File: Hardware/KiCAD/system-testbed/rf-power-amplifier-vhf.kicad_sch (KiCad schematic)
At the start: 22 parts, among them U14 GRF5604

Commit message: feat: assign 0603 passive component footprints #32 #34
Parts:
- C63, C64, C65, C66, C67, C68, C69, C70, C71, C72, C73, C74, C75, C76: footprint (none) -> Capacitor_SMD:C_0603_1608Metric
- L15, L16, L17: footprint (none) -> Inductor_SMD:L_0603_1608Metric
- R16, R17, R18: footprint (none) -> Resistor_SMD:R_0603_1608Metric
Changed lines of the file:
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@@
 			)
 		)
-		(property "Footprint" ""
+		(property "Footprint" "Capacitor_SMD:C_0603_1608Metric"
 			(at 205.74 77.47 0)
 			(effects
@@
 			)
 		)
-		(property "Footprint" ""
+		(property "Footprint" "Inductor_SMD:L_0603_1608Metric"
 			(at 71.12 83.82 0)
 			(effects
@@
 			)
 		)
-		(property "Footprint" ""
+		(property "Footprint" "Resistor_SMD:R_0603_1608Metric"
 			(at 87.884 32.766 90)
 			(effects
@@
 			)
 		)
-		(property "Footprint" ""
+		(property "Footprint" "Capacitor_SMD:C_0603_1608Metric"
 			(at 144.78 83.82 0)
 			(effects
@@
 			)
 		)
-		(property "Footprint" ""
+		(property "Footprint" "Capacitor_SMD:C_0603_1608Metric"
 			(at 158.75 77.47 0)
 			(effects
@@
 			)
 		)
-		(property "Footprint" ""
+		(property "Footprint" "Inductor_SMD:L_0603_1608Metric"
 			(at 144.78 71.12 0)
 			(effects
@@
 			)
 		)
-		(property "Footprint" ""
+		(property "Footprint" "Resistor_SMD:R_0603_1608Metric"
 			(at 138.684 63.754 90)
 			(effects
@@
 			)
 		)
-		(property "Footprint" ""
+		(property "Footprint" "Capacitor_SMD:C_0603_1608Metric"
 			(at 104.14 45.72 0)
 			(effects
@@
 			)
 		)
-		(property "Footprint" ""
+		(property "Footprint" "Capacitor_SMD:C_0603_1608Metric"
 			(at 171.45 43.18 0)
 			(effects
@@
 			)
 		)
-		(property "Footprint" ""
+		(property "Footprint" "Capacitor_SMD:C_0603_1608Metric"
 			(at 176.53 83.82 0)
 			(effects
@@
 			)
 		)
-		(property "Footprint" ""
+		(property "Footprint" "Capacitor_SMD:C_0603_1608Metric"
 			(at 73.66 45.72 0)
 			(effects
@@
 			)
 		)
-		(property "Footprint" ""
+		(property "Footprint" "Capacitor_SMD:C_0603_1608Metric"
 			(at 165.1 83.82 0)
 			(effects
@@
 			)
 		)
-		(property "Footprint" ""
+		(property "Footprint" "Capacitor_SMD:C_0603_1608Metric"
 			(at 161.29 43.18 0)
 			(effects
@@
 			)
 		)
-		(property "Footprint" ""
+		(property "Footprint" "Capacitor_SMD:C_0603_1608Metric"
 			(at 199.39 83.82 0)
 			(effects
@@
 			)
 		)
-		(property "Footprint" ""
+		(property "Footprint" "Capacitor_SMD:C_0603_1608Metric"
 			(at 187.96 83.82 0)
 			(effects
@@
 			)
 		)
-		(property "Footprint" ""
+		(property "Footprint" "Capacitor_SMD:C_0603_1608Metric"
 			(at 88.9 45.72 0)
 			(effects
@@
 			)
 		)
-		(property "Footprint" ""
+		(property "Footprint" "Capacitor_SMD:C_0603_1608Metric"
 			(at 87.63 77.47 0)
 			(effects
@@
 			)
 		)
-		(property "Footprint" ""
+		(property "Footprint" "Resistor_SMD:R_0603_1608Metric"
 			(at 72.644 32.766 90)
 			(effects
@@
 			)
 		)
-		(property "Footprint" ""
+		(property "Footprint" "Inductor_SMD:L_0603_1608Metric"
 			(at 114.3 45.72 0)
 			(effects
@@
 			)
 		)
-		(property "Footprint" ""
+		(property "Footprint" "Capacitor_SMD:C_0603_1608Metric"
 			(at 77.47 77.47 0)
 			(effects

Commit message: fix: import RF sheet contents #65
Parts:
- renumbered C63 to C56, C64 to C57, C65 to C58, C66 to C59, C67 to C60, C68 to C61, C69 to C62, C70 to C63, C71 to C64, C72 to C65, C73 to C66, C74 to C67, C75 to C68, C76 to C69, L15 to L22, L16 to L23, L17 to L24, U14 to U4

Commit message: fix: reannotate schematics for pcb editor use #55
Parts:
- L36: renamed from L22; footprint Inductor_SMD:L_0603_1608Metric -> Inductor_SMD:L_0402_1005Metric
- L37: renamed from L23; footprint Inductor_SMD:L_0603_1608Metric -> Inductor_SMD:L_0402_1005Metric
- L38: renamed from L24; footprint Inductor_SMD:L_0603_1608Metric -> Inductor_SMD:L_0402_1005Metric
- renumbered C56 to C80, C57 to C81, C58 to C82, C59 to C83, C60 to C84, C61 to C85, C62 to C86, C63 to C87, C64 to C88, C65 to C89, C66 to C90, C67 to C91, C68 to C92, C69 to C93, JP10 to JP9, R16 to R17, R17 to R18, R18 to R19, U4 to U6

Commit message: fix: allow for DRC use in PCB editor by successful reannotation
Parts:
- C80, C81, C82, C83, C84, C85, C87, C88, C89, C90, C91, C92, C93: footprint Capacitor_SMD:C_0603_1608Metric -> Capacitor_SMD:C_0402_1005Metric
- L86: renamed from C86; footprint Capacitor_SMD:C_0603_1608Metric -> Inductor_SMD:L_0402_1005Metric
- R17, R18, R19: footprint Resistor_SMD:R_0603_1608Metric -> Resistor_SMD:R_0402_1005Metric
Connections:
- net +5V renamed +3.3V

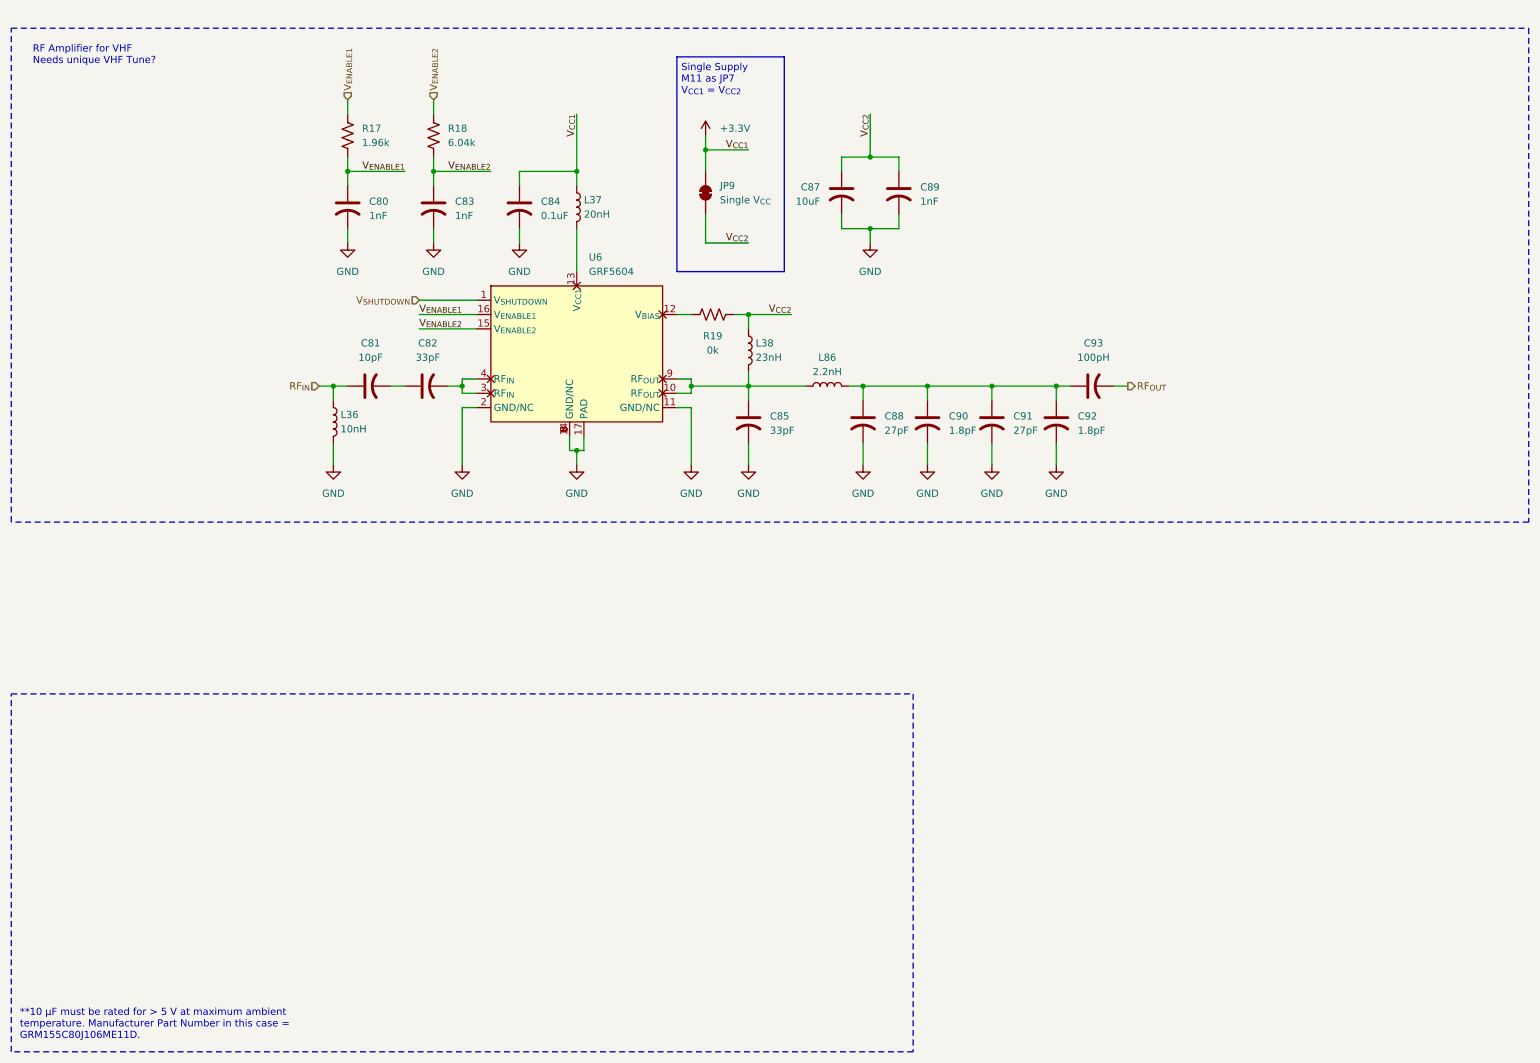
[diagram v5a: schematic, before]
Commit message: feat: separate RF subsystems for testing using SMA edge launches in testbed KiCAD project #65 #34 #45
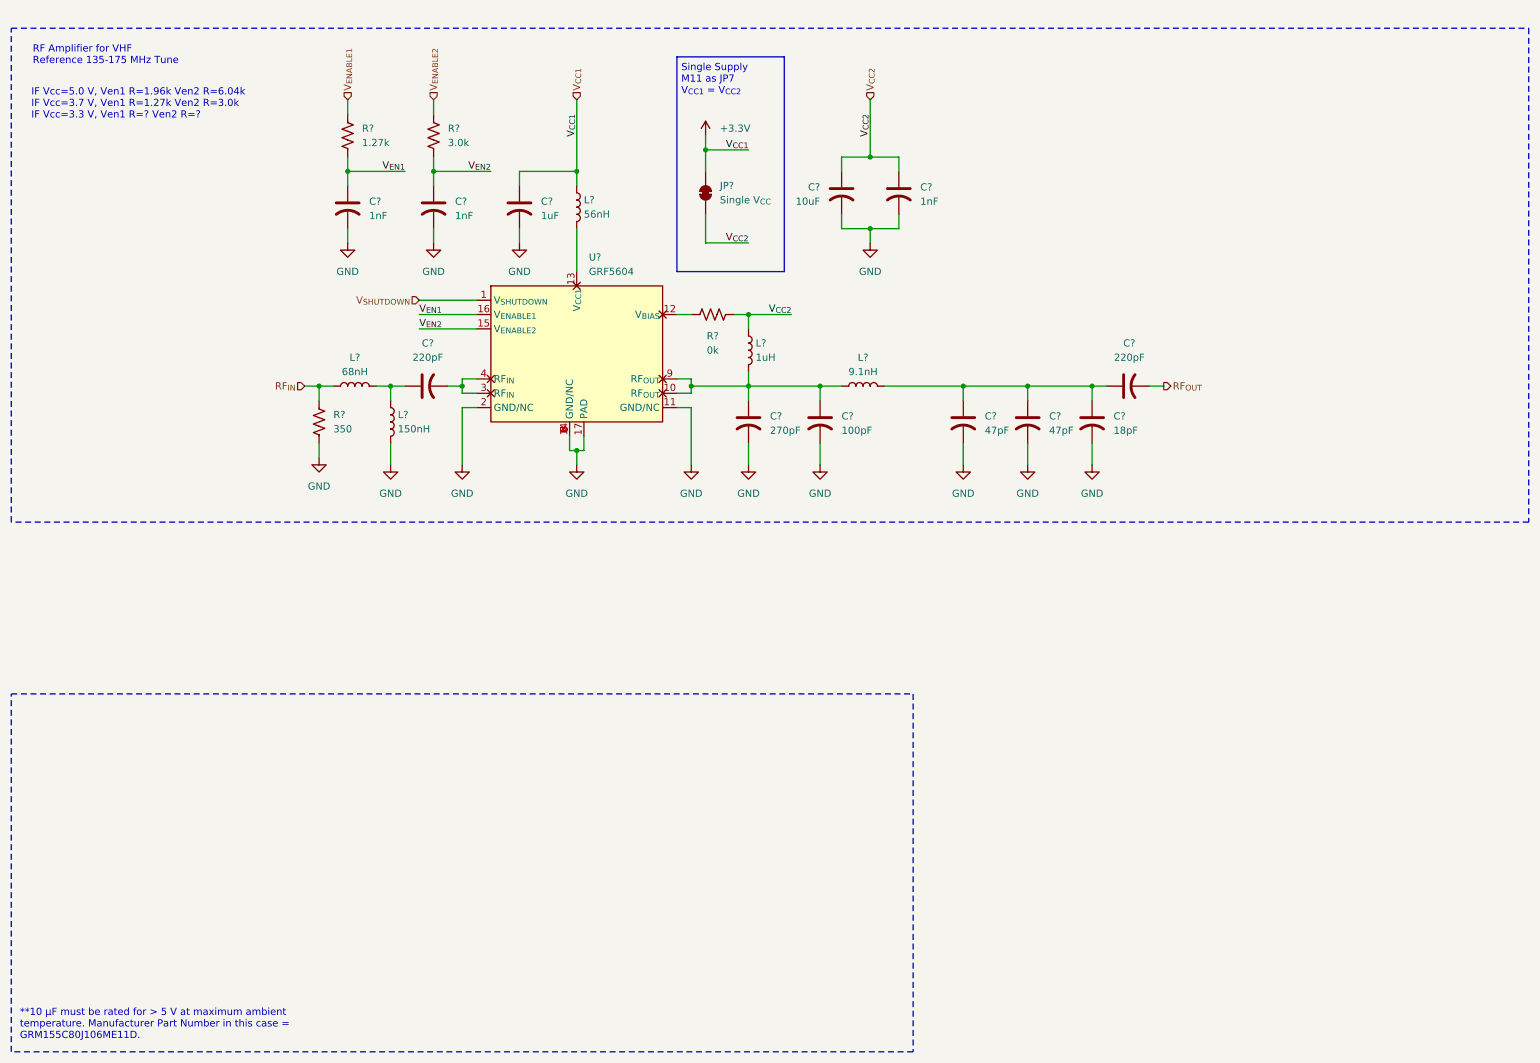
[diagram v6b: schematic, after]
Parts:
- added R?: 350, Resistor_SMD:R_0402_1005Metric, symbol Device:R_US
- C?: renamed from C93; value 100pH -> 220pF
- C?: renamed from C85; value 33pF -> 270pF
- C?: renamed from C84; value 0.1uF -> 1uF
- C?: renamed from C90; value 1.8pF -> 47pF
- C?: renamed from C88; value 27pF -> 100pF
- C?: renamed from C92; value 1.8pF -> 18pF
- C?: renamed from C91; value 27pF -> 47pF
- C?: renamed from C82; value 33pF -> 220pF
- L?: renamed from L36; value 10nH -> 150nH
- L?: renamed from L86; value 2.2nH -> 9.1nH
- L?: renamed from L38; value 23nH -> 1uH; footprint Inductor_SMD:L_0402_1005Metric -> capstone-project:IND_IMSC1008AZER_VIS
- L?: renamed from L37; value 20nH -> 56nH
- L?: renamed from C81; value 10pF -> 68nH; footprint Capacitor_SMD:C_0402_1005Metric -> Inductor_SMD:L_0402_1005Metric; symbol Device:C_US -> Device:L
- R?: renamed from R18; value 6.04k -> 3.0k
- R?: renamed from R17; value 1.96k -> 1.27k
- renumbered C89 to C?, C80 to C?, C87 to C?, C83 to C?, JP9 to JP?, R19 to R?, U6 to U?
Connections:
- net GND: now also R?.1
- net RF_{IN}: now also R?.2; no longer L?.1
- net V_{ENABLE1}: no longer C?.1, R?.1, U?.16 (V_{ENABLE1})
- net V_{ENABLE2}: no longer C?.1, R?.1, U?.15 (V_{ENABLE2})
- net at C?.1, C?.1, C?.1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: no longer C?.1
- net at C?.1, L?.1, L?.2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: now also C?.1
- net at C?.1, L?.2: now also L?.1
- new net V_{EN1}: C?.1, R?.1, U?.16 (V_{ENABLE1})
- new net V_{EN2}: C?.1, R?.1, U?.15 (V_{ENABLE2})
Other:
- note added: "IF Vcc=5.0 V, Ven1 R=1.96k Ven2 R=6.04k IF Vcc=3.7 V, Ven1 R=1.27k Ven2 R=3.0k IF Vcc=3.3 V, Ven1 R=? Ven2 R=?"
- note added: "RF Amplifier for VHF Reference 135-175 MHz Tune"
- note removed: "RF Amplifier for VHF Needs unique VHF Tune?"
- moved on the sheet: C?, L?
